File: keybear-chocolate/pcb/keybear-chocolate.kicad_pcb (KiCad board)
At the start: 2 copper layers, 151.4 x 117.1 mm, 95 parts, among them J1 MJ-4PP-9, J2 BATT, J3 LED, J4 OLED, SW1 SW_PUSH, SW10 SW_PUSH, SW11 SW_PUSH, SW12 SW_PUSH, SW13 SW_PUSH, SW14 SW_PUSH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

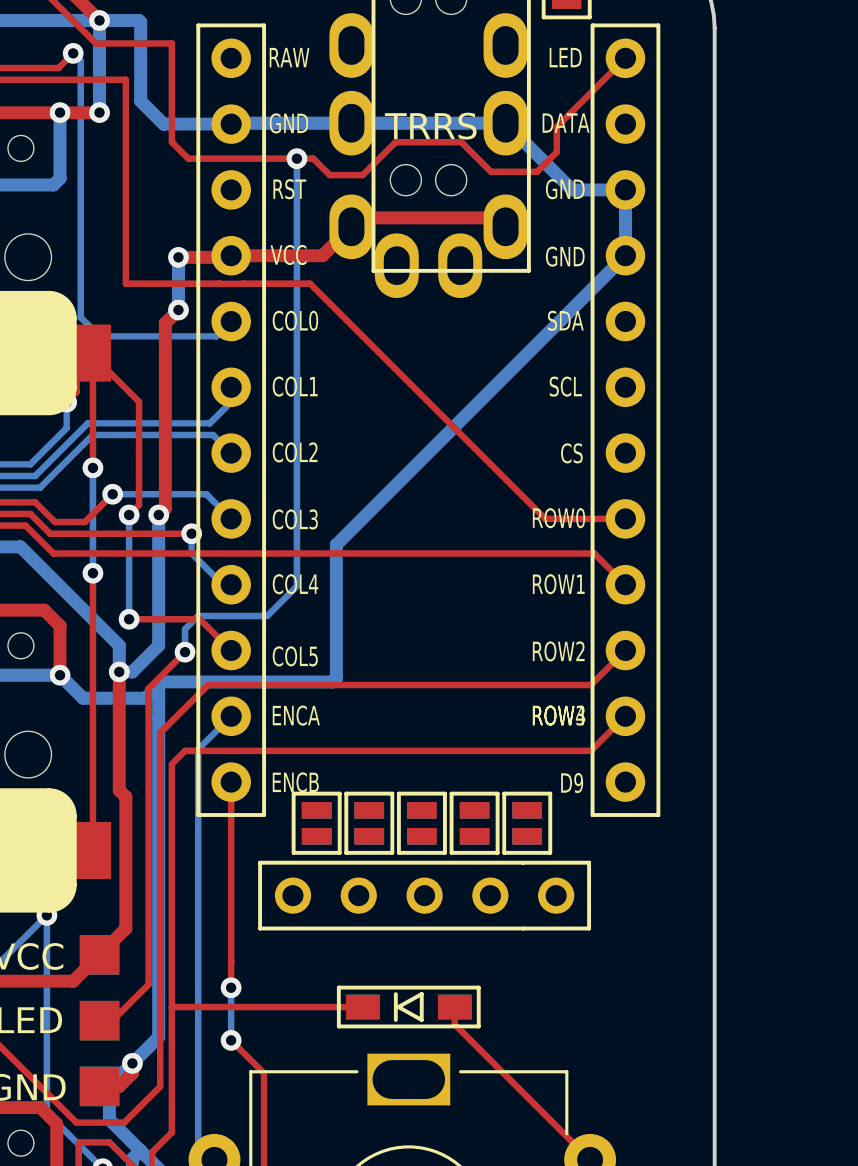
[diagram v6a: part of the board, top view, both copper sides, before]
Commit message: OLED Jumper fixed and connected
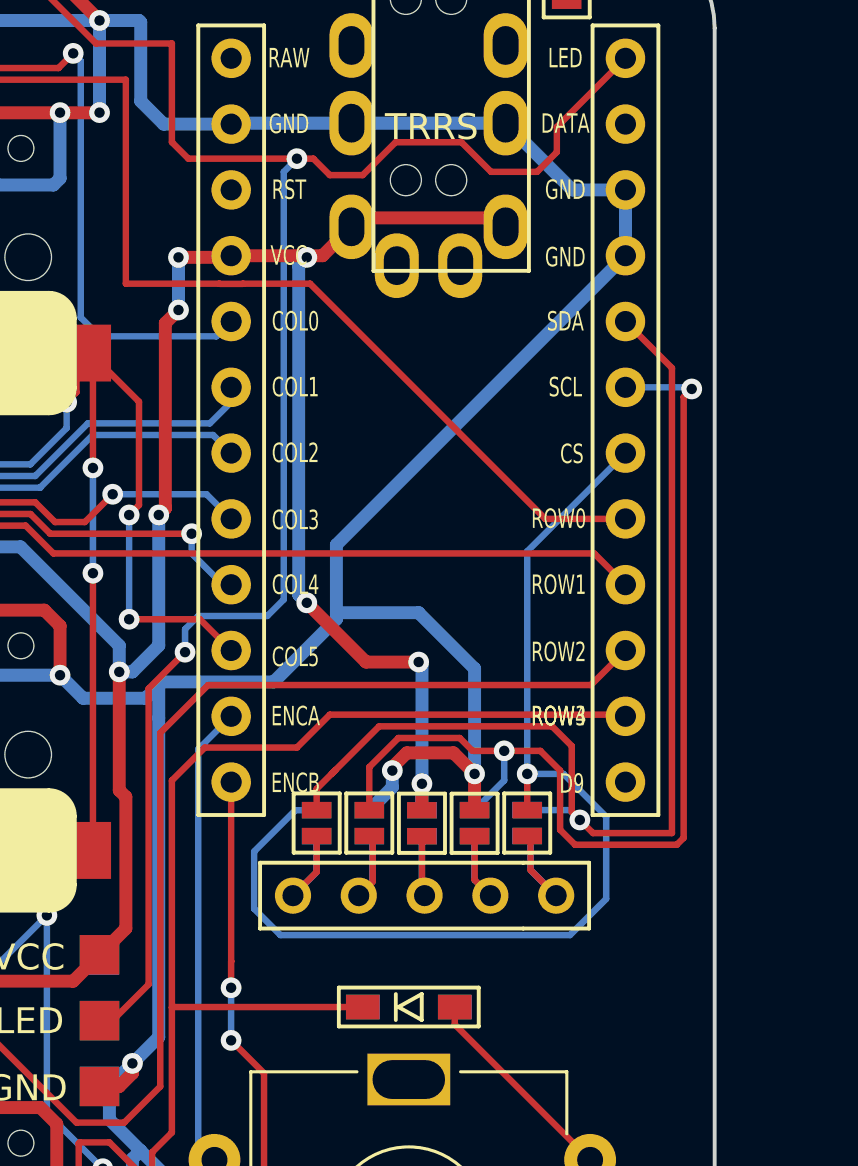
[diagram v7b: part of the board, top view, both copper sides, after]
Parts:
- JP10: footprint kbd:Jumper -> SofleKeyboard-footprint:Jumper
- moved JP6 8.13 mm to (270.8, 129.5)
- moved JP11 8.13 mm to (262.6, 129.5)
- moved JP7 4.06 mm to (268.7, 129.5)
- moved JP9 4.06 mm to (264.7, 129.5)
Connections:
- JP11 pad 2: Net-(J4-Pin_5) -> Net-(J4-Pin_1)
- JP6 pad 2: Net-(J4-Pin_4) -> Net-(J4-Pin_5)
- JP7 pad 2: Net-(J4-Pin_3) -> Net-(J4-Pin_4)
- JP8 pad 2: Net-(J4-Pin_2) -> Net-(J4-Pin_3)
- JP9 pad 2: Net-(J4-Pin_1) -> Net-(J4-Pin_2)
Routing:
- net CS: track 0.00 -> 42.1 mm, vias 0 -> 1
- net SDA: track 0.00 -> 41.6 mm, vias 0 -> 1
- net SCL: track 0.00 -> 40.2 mm, vias 0 -> 2
- net VCC: track 893.4 -> 919.2 mm, vias 55 -> 59
- net GND: track 935.7 -> 952.1 mm, vias 32 -> 34
- net Net-(J4-Pin_5): track 0.00 -> 6.06 mm
- net Net-(J4-Pin_2): track 0.00 -> 5.72 mm
- net Net-(J4-Pin_1): track 0.00 -> 5.35 mm
- net Net-(J4-Pin_4): track 0.00 -> 5.10 mm
- net Net-(J4-Pin_3): track 0.00 -> 4.67 mm

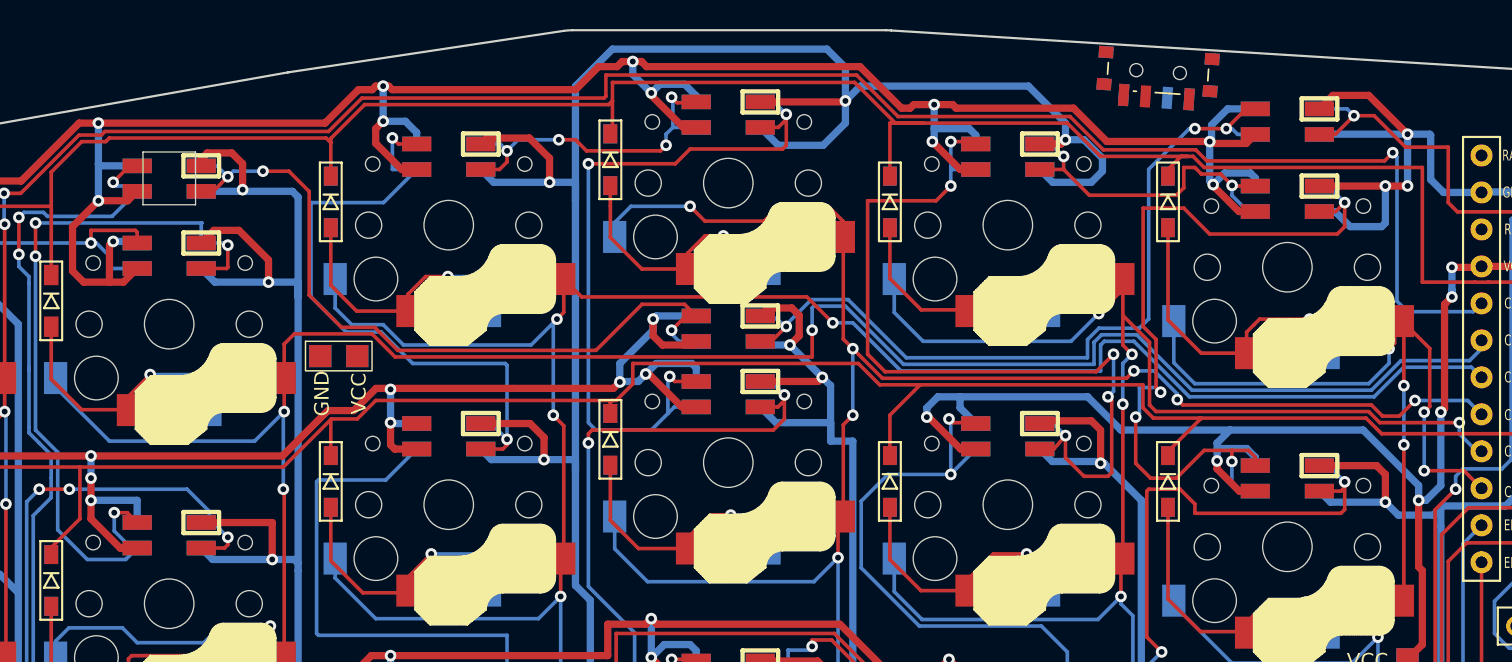
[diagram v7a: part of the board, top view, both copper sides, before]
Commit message: batt strip connection updated. tracks made
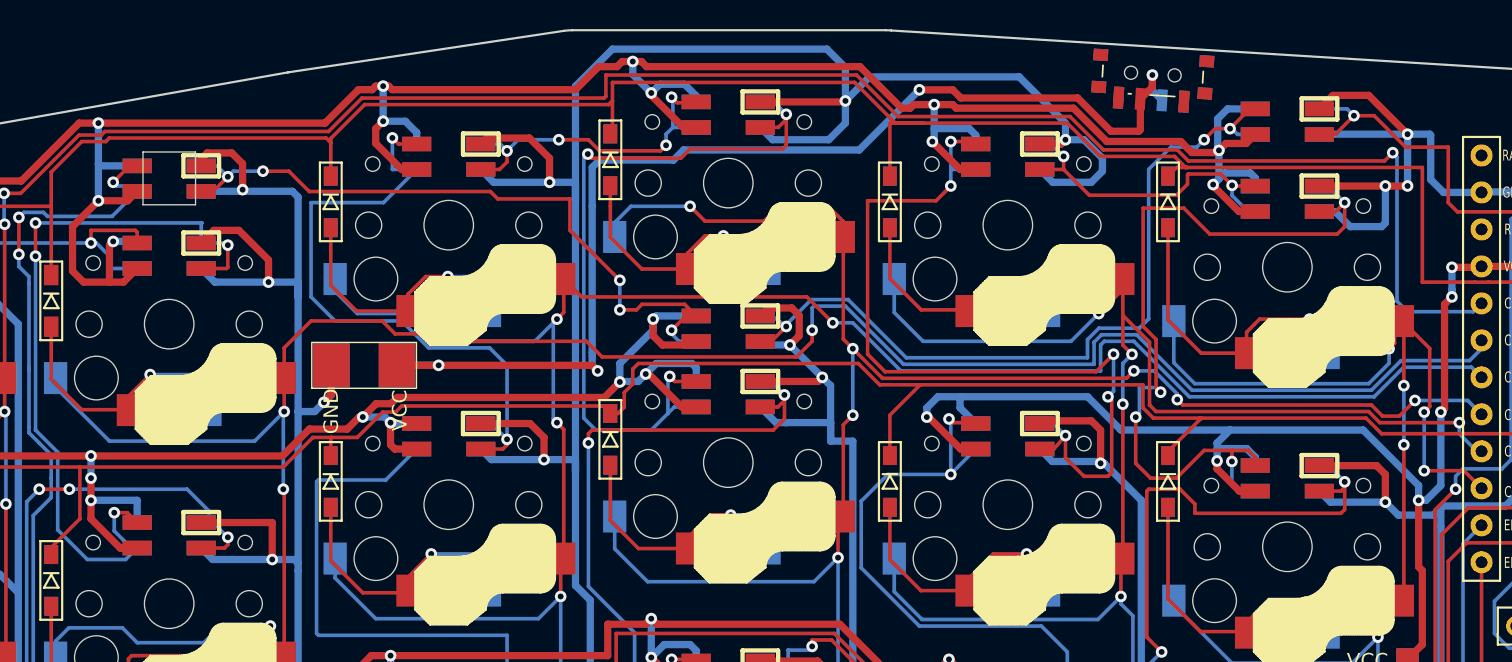
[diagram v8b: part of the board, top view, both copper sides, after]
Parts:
- moved J2 0.99 mm to (180.3, 114.4)
- moved SW30 0.40 mm to (236.7, 94.8), turned to -3.5 degrees
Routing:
- net BATT_VCC: track 0.00 -> 78.4 mm, vias 0 -> 4
- net GND: track 952.1 -> 959.8 mm, vias 34 -> 35
- net Net-(L28-DIN): track 51.9 -> 47.9 mm, vias 3 -> 5
- net row1: track 165.5 -> 164.1 mm
- net Net-(L10-DOUT): track 51.6 -> 52.5 mm
- net col2: track 263.0 -> 262.2 mm
- net Net-(L5-DIN): track 23.3 -> 22.5 mm
- net row0: track 175.8 -> 175.2 mm
